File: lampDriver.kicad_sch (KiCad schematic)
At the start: 73 parts, among them IC8 1ED44175N01BXTSA1, Q4 DCX114EU-7-F, Q5 DCX114EU-7-F, T1 T_NMOS_DSKG, U1 LM2901, U3 OPA2356AIDGKR

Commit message: Final Rev. 1.0.0
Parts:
- C41: value 100p 0603 -> 100n 0603
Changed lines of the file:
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@@
 			)
 		)
-		(property "Value" "100p 0603"
+		(property "Value" "100n 0603"
 			(at 27.686 72.136 0)
 			(effects

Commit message: Final Version Rev. 2.0.0
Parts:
- added M2: KU-CG20, Hansmann_Kühlkörper:GapPad_19mm, symbol Hansmann_Kühlkörper:Gappad
- C42: value 220µ 35V -> DNP
- C43, C45, C47, C56: value 10µ X7R 50V 1210 -> 10µ X7R 1210
- C54: value 100p 0603 -> 100n 0603
- M1: value ~ -> K 274 MI 247 V
- T101: renamed from T1; value T_NMOS_DSKG -> IMZC120R078M2H
- TH1: Article (none) -> B59721A0070A062
- renumbered U3 to IC1, U1 to IC2, L6 to L101, Q4 to T4, Q5 to T5
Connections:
- net at R59.2, VR1.2: no longer VR1.3
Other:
- moved on the sheet: C48, C51, M1, R61, R69, VR1

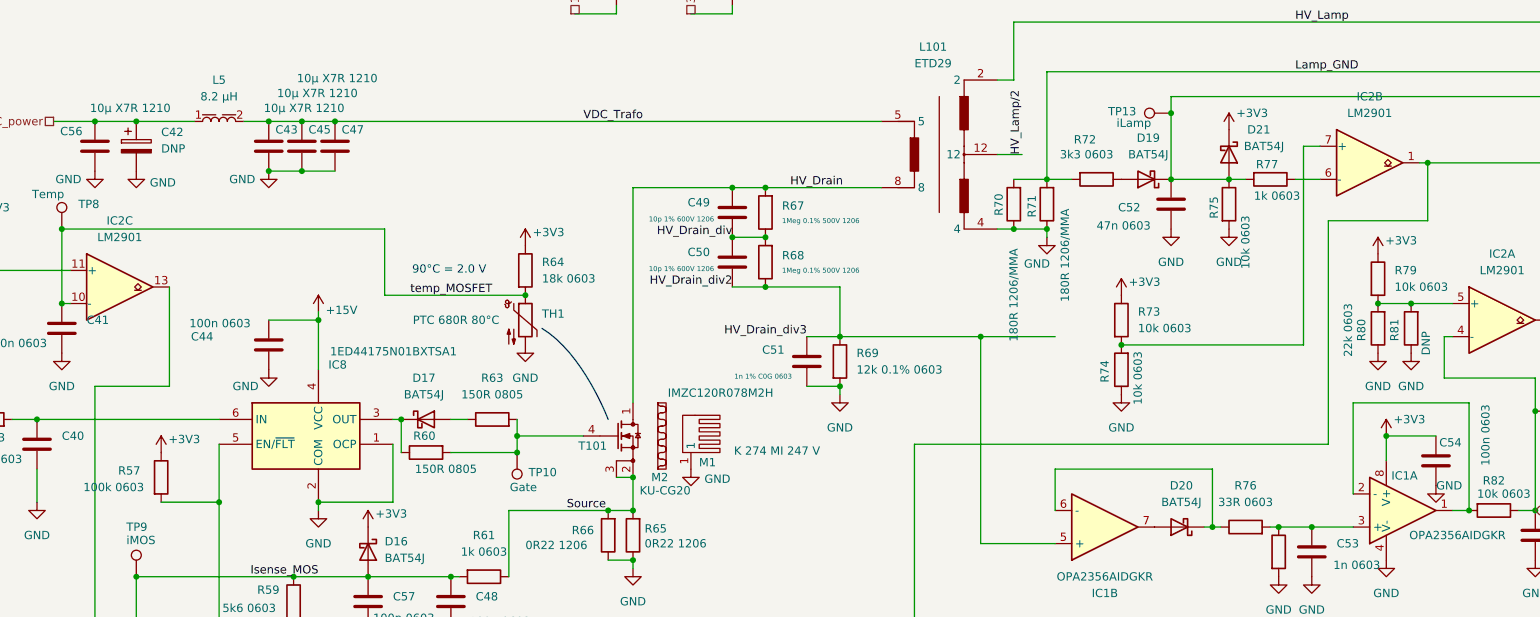
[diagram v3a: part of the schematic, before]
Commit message: Fixed BoM, and added jobset.
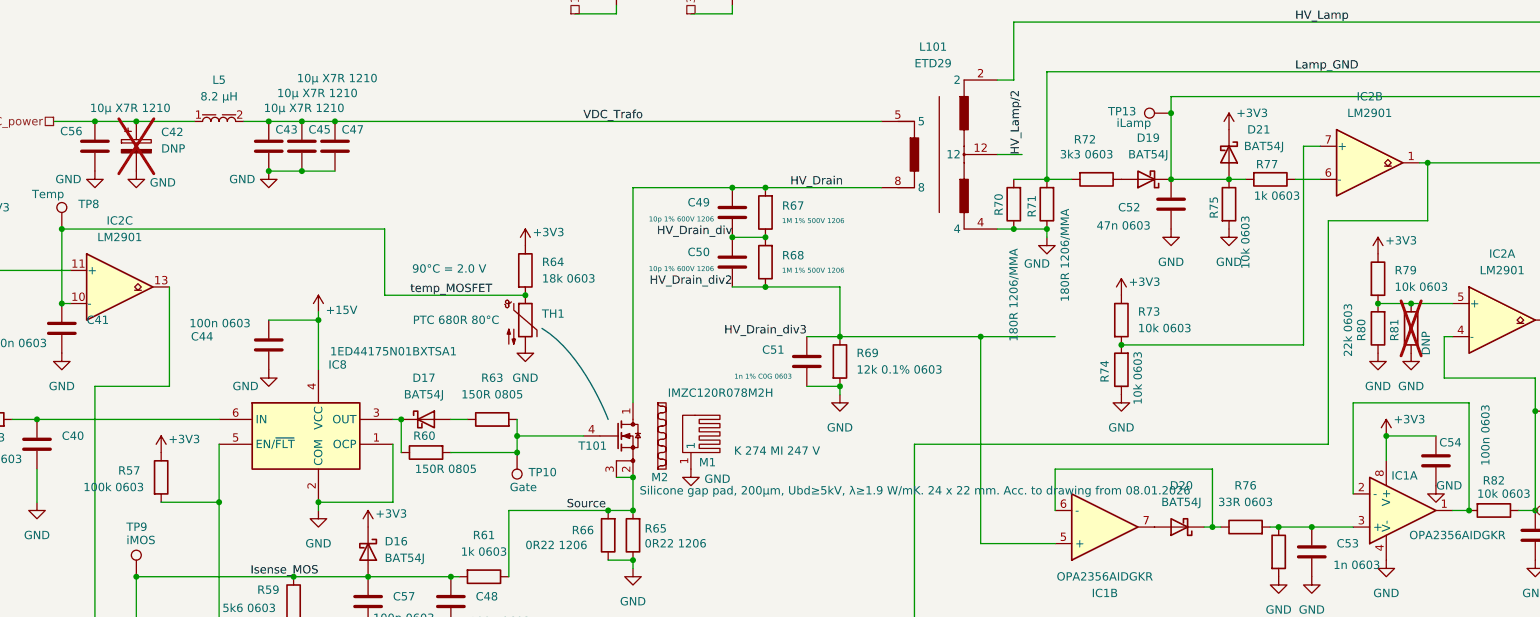
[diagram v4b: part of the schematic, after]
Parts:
- C40, C48, C57: LCSC Part Number (none) -> C296717; Manufacturer_Part_Number (none) -> CL10C101JC8NNNC
- C41, C44, C46, C54: LCSC Part Number (none) -> C15725; Manufacturer_Part_Number (none) -> CL10B104KC8NNNC
- C42, R81: now not fitted; now left out of the parts list
- C43, C45, C47, C56: LCSC Part Number (none) -> C138687; Manufacturer_Part_Number (none) -> CL32B106KBJNNNE
- C49, C50: LCSC Part Number (none) -> C107172; Manufacturer_Part_Number (none) -> CC1206JKNPOCBN100
- C51: LCSC Part Number (none) -> C576765; Manufacturer_Part_Number (none) -> CC0603FRNPO0BN102
- C52: LCSC Part Number (none) -> C307354; Manufacturer_Part_Number (none) -> CL10B473KC8WPNC
- C53: LCSC Part Number (none) -> C153291; Manufacturer_Part_Number (none) -> CL10B102KC8NNNC
- C55: LCSC Part Number (none) -> C5199872; Manufacturer_Part_Number (none) -> CL10B105KB8NQNC
- D16, D17, D18, D19, D20, D21: LCSC Part Number (none) -> C86299; Manufacturer_Part_Number (none) -> BAT54JFILM
- IC1: LCSC Part Number (none) -> C2057371; Manufacturer_Part_Number (none) -> OPA2356AIDGKR
- IC2: LCSC Part Number (none) -> C54868; Manufacturer_Part_Number (none) -> LM2901PWR
- IC8: LCSC Part Number (none) -> C530933; Manufacturer_Part_Number 1ED44175N01BXTSA1 -> 1ED44175N01B
- L5: Manufacturer_Part_Number (none) -> 744045008
- M1: Manufacturer_Part_Number (none) -> FK 274 MI 247 V
- M2: value KU-CG20 -> Silicone gap pad, 200µm, Ubd≥5kV, λ≥1.9 W/mK. 24 x 22 mm. Acc. to drawing from 08.01.2026; Manufacturer_Part_Number (none) -> KU-CG20
- R52, R55, R58, R73, R74, R75, R79, R82: LCSC Part Number (none) -> C98220; Manufacturer_Part_Number (none) -> RC0603FR-0710KL
- R53: LCSC Part Number (none) -> C125931; Manufacturer_Part_Number (none) -> AC0603FR-072K2L
- R54: LCSC Part Number (none) -> C105588; Manufacturer_Part_Number (none) -> RC0603FR-07100RL
- R56, R72: LCSC Part Number (none) -> C108078; Manufacturer_Part_Number (none) -> RC0603FR-073K3L
- R57: LCSC Part Number (none) -> C14675; Manufacturer_Part_Number (none) -> RC0603FR-07100KL
- R59: LCSC Part Number (none) -> C114627; Manufacturer_Part_Number (none) -> RC0603FR-075K6L
- R60, R63: LCSC Part Number (none) -> C114523; Manufacturer_Part_Number (none) -> RC0805FR-07150RL
- R61, R62, R77: LCSC Part Number (none) -> C22548; Manufacturer_Part_Number (none) -> RC0603FR-071KL
- R64: LCSC Part Number (none) -> C114610; Manufacturer_Part_Number (none) -> RC0603FR-0718KL
- R65, R66: LCSC Part Number (none) -> C155692; Manufacturer_Part_Number (none) -> RL1206FR-070R22L
- R67, R68: value 1Meg 0.1% 500V 1206 -> 1M 1% 500V 1206; LCSC Part Number (none) -> C253347; Manufacturer_Part_Number (none) -> KTR18EZPF1004
- R69: LCSC Part Number (none) -> C326735; Manufacturer_Part_Number (none) -> RT0603BRD0712KL
- R70, R71: LCSC Part Number (none) -> C2928662; Manufacturer_Part_Number (none) -> MMA02040C1800FB300
- R76: LCSC Part Number (none) -> C108661; Manufacturer_Part_Number (none) -> RC0603FR-0733RL
- R78: LCSC Part Number (none) -> C114606; Manufacturer_Part_Number (none) -> RC0603FR-0710ML
- R80: LCSC Part Number (none) -> C114065; Manufacturer_Part_Number (none) -> RC0603FR-0722KL
- T101: LCSC Part Number (none) -> C44184296; Manufacturer_Part_Number (none) -> IMZC120R078M2HXKSA1
- T4, T5: LCSC Part Number (none) -> C460018
- TH1: LCSC Part Number (none) -> C2655235; Manufacturer_Part_Number (none) -> B59721A0080A062
- TP10, TP11, TP12, TP13, TP14, TP8, TP9: now left out of the parts list
- VR1: LCSC Part Number (none) -> C719176

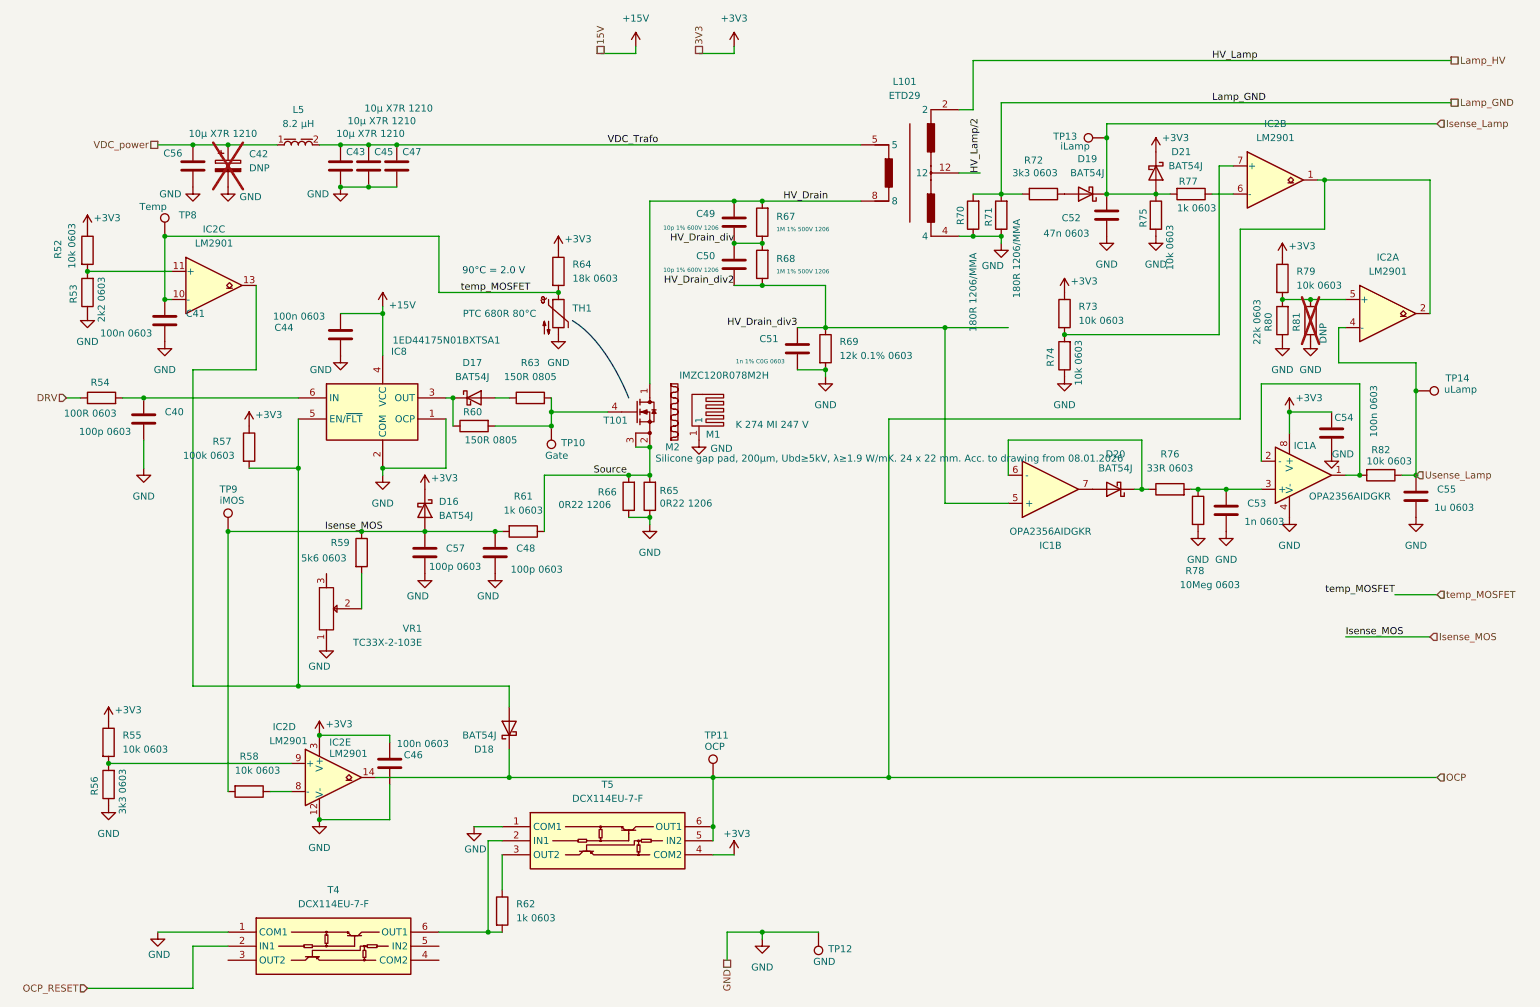
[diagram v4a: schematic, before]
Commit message: Fixed debug header footprint, and cleaned up silkscreen.
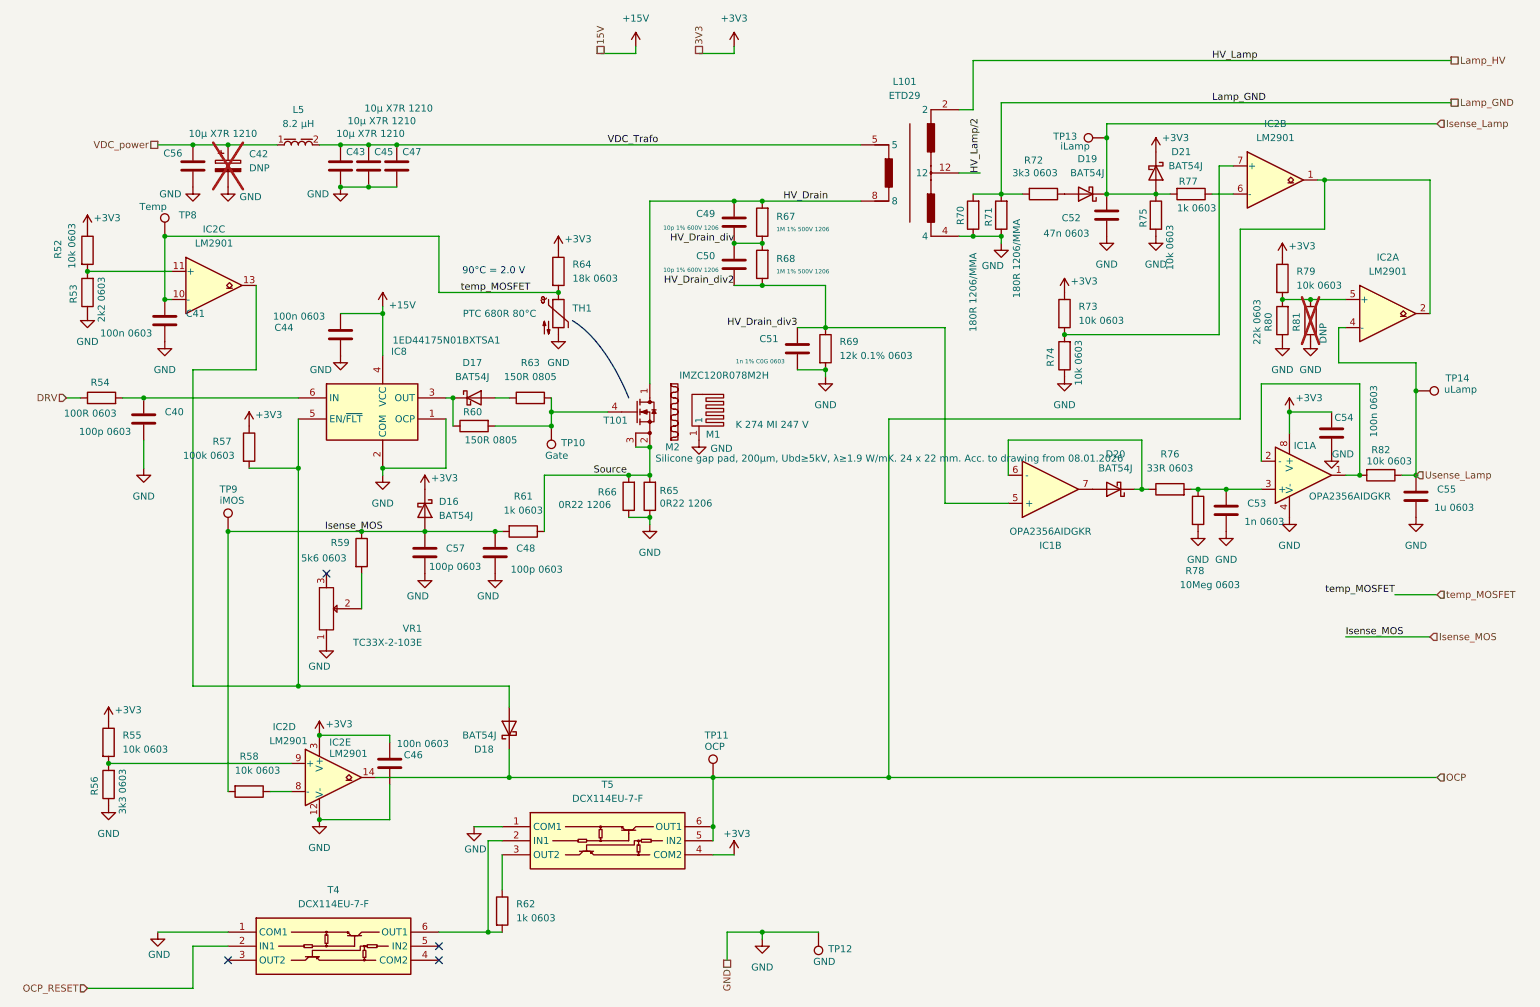
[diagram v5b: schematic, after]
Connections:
- no-connect marks 0 -> 4
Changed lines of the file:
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@@
-	)
-	(junction
-		(at 180.34 71.12)
-		(diameter 0)
-		(color 0 0 0 0)
 	)
 	(junction
@@
 		(color 0 0 0 0)
 	)
+	(no_connect
+		(at 68.58 115.57)
+	)
+	(no_connect
+		(at 88.9 182.88)
+	)
+	(no_connect
+		(at 88.9 185.42)
+	)
+	(no_connect
+		(at 50.8 185.42)
+	)
 	(wire
 		(pts
@@
 		)
 		(stroke
-			(width 0)
-			(type default)
-		)
-	)
-	(wire
-		(pts
-			(xy 180.34 71.12) (xy 191.77 71.12)
-		)
-		(stroke

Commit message: Fixed transformer footprint, and cleaned up silkscreen.
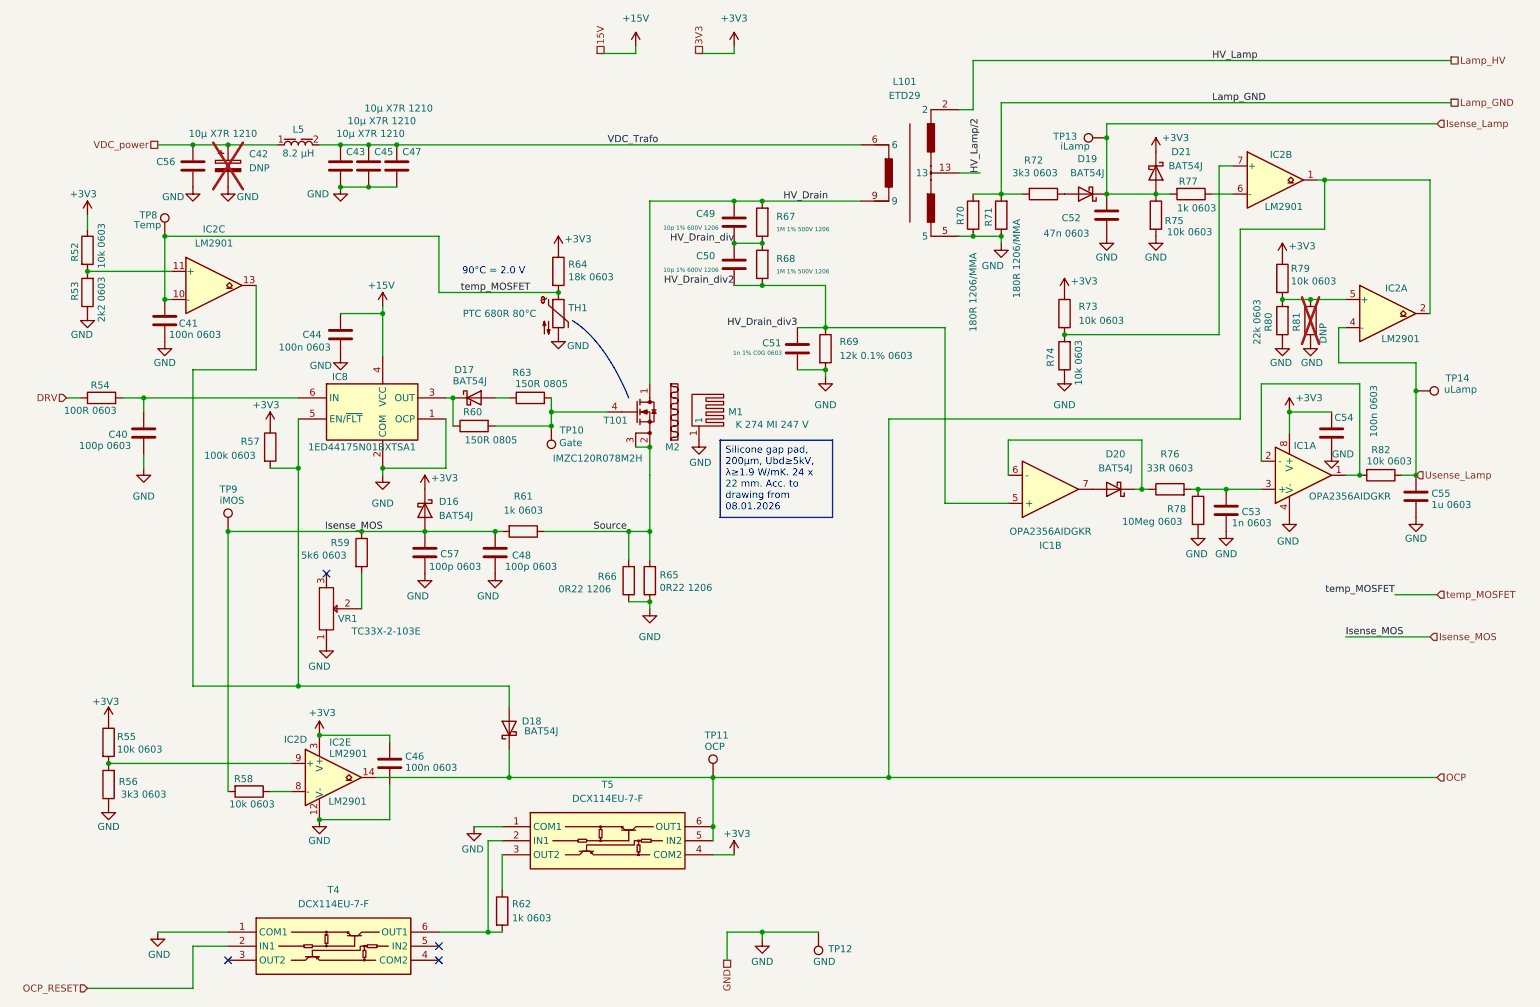
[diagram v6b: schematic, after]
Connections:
- net GND: now also L101.5; no longer L101.4
- net HV_Drain: now also L101.9; no longer L101.8
- net HV_Lamp/2: now also L101.13; no longer L101.12
- net VDC_Trafo: now also L101.6; no longer L101.5
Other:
- moved on the sheet: C40, R57, R65, R66
